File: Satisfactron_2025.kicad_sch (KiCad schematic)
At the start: 147 parts, among them J1 USB-TYPE-C-018, J10 GT-BTP30002-0350B-019B, J11 Conn_01x03, J12 LED strip, J2 GT-BTP30002-0350B-019B, J3 TF_PUSH, J4 GT-BTP30002-0350B-019B, J5 PZ254V-11-04P_C2691448, J6 Conn_01x06, J7 GT-BTP30002-0350B-019B, J8 GT-BTP30002-0350B-019B, J9 GT-BTP30002-0350B-019B, Q1 2N7002, SW1 MSK-22D18G4_051, SW10 SPVN310101, SW11 SPVN310101, SW12 SPVN310101, SW13 SPVN310101, SW14 SPVN310101, SW15 SPVN310101, SW2 TS-1088-AR02016, SW3 SPVN310101, SW4 SPVN310101, SW5 TS-1088-AR02016, SW6 TS-1088-AR02016, SW7 TS-1088-AR02016, SW8 SPVN310101, SW9 SPVN310101, U1 AMS1117-3.3, U10 WS2811C, U11 WS2811C, U12 WS2811C, U13 WS2811C, U14 TSSP77038TT, U2 TPS82130, U3 ESP32-S3-WROOM-1-N16R8, U4 TSSP77038TR, U5 TSSP77038TR, U6 TSSP77038TR, U7 TSSP77038TR, U8 TSSP77038TR, U9 WS2811C

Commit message: Minor corrections
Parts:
- added SW16, SW17, SW18, SW19, SW20: SPVN310101, Switch_KSL:SW-SMD_SPVN310101, symbol Switch_KSL:SPVN310101
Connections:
- no-connect marks 31 -> 51

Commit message: RC last check, silkscreen done
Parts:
- U1: LCSC C7376 -> C6186
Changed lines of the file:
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@@
 			)
 		)
-		(property "LCSC" "C7376"
+		(property "LCSC" "C6186"
 			(at 52.07 161.925 0)
 			(effects

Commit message: Production file (incl. Step)
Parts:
- C18, C19, C20, C21, C24: LCSC (none) -> C14663
- D2: LCSC C2286 -> C2290
- Q1: LCSC (none) -> C8545
- R1, R3: LCSC (none) -> C23186
- R11: LCSC C25804 -> C23162
- R15, R16, R17, R8, R9: LCSC C23182 -> C22808
- R19: LCSC (none) -> C21190
- R21, R22, R26, R32, R33, R34, R35, R36, R37, R38, R39, R40, R41, R42, R5, R6, R7: LCSC C23182 -> C23140
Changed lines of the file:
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@@
 			)
 		)
-		(property "LCSC" "C23182"
+		(property "LCSC" "C22808"
 			(at 288.29 53.34 0)
 			(effects
@@
 			)
 		)
-		(property "LCSC" "C23182"
+		(property "LCSC" "C23140"
 			(at 260.35 58.42 0)
 			(effects
@@
 			)
 		)
-		(property "LCSC" "C23182"
+		(property "LCSC" "C23140"
 			(at 311.15 60.96 0)
 			(effects
@@
 			)
 		)
-		(property "LCSC" "C23182"
+		(property "LCSC" "C23140"
 			(at 360.68 60.96 0)
 			(effects
@@
 			)
 		)
-		(property "LCSC" "C23182"
+		(property "LCSC" "C23140"
 			(at 151.13 58.42 0)
 			(effects
@@
 			)
 		)
-		(property "LCSC" "C23182"
+		(property "LCSC" "C23140"
 			(at 200.66 63.5 0)
 			(effects
@@
 			)
 		)
+		(property "LCSC" "C21190"
+			(at 88.9 255.27 0)
+			(effects
+				(font
+					(size 1.27 1.27)
+				)
+				(hide yes)
+			)
+		)
 		(pin "1"
 		)
@@
 			)
 		)
-		(property "LCSC" "C23182"
+		(property "LCSC" "C22808"
 			(at 233.68 53.34 0)
 			(effects
@@
 			)
 		)
-		(property "LCSC" "C23182"
+		(property "LCSC" "C23140"
 			(at 308.61 63.5 0)
 			(effects
@@
 			)
 		)
-		(property "LCSC" "C23182"
+		(property "LCSC" "C23140"
 			(at 17.78 212.09 0)
 			(effects
@@
 			)
 		)
-		(property "LCSC" "C23182"
+		(property "LCSC" "C23140"
 			(at 205.74 58.42 0)
 			(effects
@@
 			)
 		)
-		(property "LCSC" "C25804"
+		(property "LCSC" "C23162"
 			(at 120.65 195.58 0)
 			(effects
@@
 			)
 		)
+		(property "LCSC" "C14663"
+			(at 295.91 59.6835 0)
+			(effects
+				(font
+					(size 1.27 1.27)
+				)
+				(hide yes)
+			)
+		)
 		(pin "1"
 		)
@@
 			)
 		)
-		(property "LCSC" "C23182"
+		(property "LCSC" "C23140"
 			(at 146.05 63.5 0)
 			(effects
@@
 			)
 		)
+		(property "LCSC" "C8545"
+			(at 141.732 193.548 0)
+			(effects
+				(font
+					(size 1.27 1.27)
+				)
+				(hide yes)
+			)
+		)
 		(pin "3"
 		)
@@
 			)
 		)
-		(property "LCSC" "C23182"
+		(property "LCSC" "C23140"
 			(at 203.2 60.96 0)
 			(effects
@@
 			)
 		)
-		(property "LCSC" "C23182"
+		(property "LCSC" "C22808"
 			(at 391.16 53.34 0)
 			(effects
@@
 			)
 		)
-		(property "LCSC" "C23182"
+		(property "LCSC" "C23140"
 			(at 257.81 60.96 0)
 			(effects
@@
 			)
 		)
+		(property "LCSC" "C14663"
+			(at 349.25 59.6835 0)
+			(effects
+				(font
+					(size 1.27 1.27)
+				)
+				(hide yes)
+			)
+		)
 		(pin "1"
 		)
@@
 			)
 		)
+		(property "LCSC" "C14663"
+			(at 186.69 54.6035 0)
+			(effects
+				(font
+					(size 1.27 1.27)
+				)
+				(hide yes)
+			)
+		)
 		(pin "1"
 		)
@@
 			)
 		)
-		(property "LCSC" "C23182"
+		(property "LCSC" "C22808"
 			(at 179.07 49.53 0)
 			(effects
@@
 			)
 		)
-		(property "LCSC" "C23182"
+		(property "LCSC" "C23140"
 			(at 148.59 60.96 0)
 			(effects
@@
 			)
 		)
-		(property "LCSC" "C23182"
+		(property "LCSC" "C23140"
 			(at 363.22 58.42 0)
 			(effects
@@
 			)
 		)
+		(property "LCSC" "C14663"
+			(at 241.3 59.6835 0)
+			(effects
+				(font
+					(size 1.27 1.27)
+				)
+				(hide yes)
+			)
+		)
 		(pin "1"
 		)
@@
 			)
 		)
-		(property "LCSC" ""
+		(property "LCSC" "C23186"
 			(at 20.32 138.43 0)
 			(effects
@@
 			)
 		)
-		(property "LCSC" "C2286"
+		(property "LCSC" "C2290"
 			(at 76.2 210.82 0)
 			(effects
@@
 			)
 		)
+		(property "LCSC" "C14663"
+			(at 398.78 59.6835 0)
+			(effects
+				(font
+					(size 1.27 1.27)
+				)
+				(hide yes)
+			)
+		)
 		(pin "1"
 		)
@@
 			)
 		)
-		(property "LCSC" "C23182"
+		(property "LCSC" "C23140"
 			(at 392.43 73.66 0)
 			(effects
@@
 			)
 		)
-		(property "LCSC" "C23182"
+		(property "LCSC" "C23140"
 			(at 313.69 58.42 0)
 			(effects
@@
 			)
 		)
-		(property "LCSC" "C23182"
+		(property "LCSC" "C22808"
 			(at 341.63 53.34 0)
 			(effects
@@
 			)
 		)
-		(property "LCSC" "C23182"
+		(property "LCSC" "C23140"
 			(at 358.14 63.5 0)
 			(effects
@@
 			)
 		)
-		(property "LCSC" "C23182"
+		(property "LCSC" "C23140"
 			(at 255.27 63.5 0)
 			(effects
@@
 			)
 		)
-		(property "LCSC" ""
+		(property "LCSC" "C23186"
 			(at 67.31 138.43 0)
 			(effects

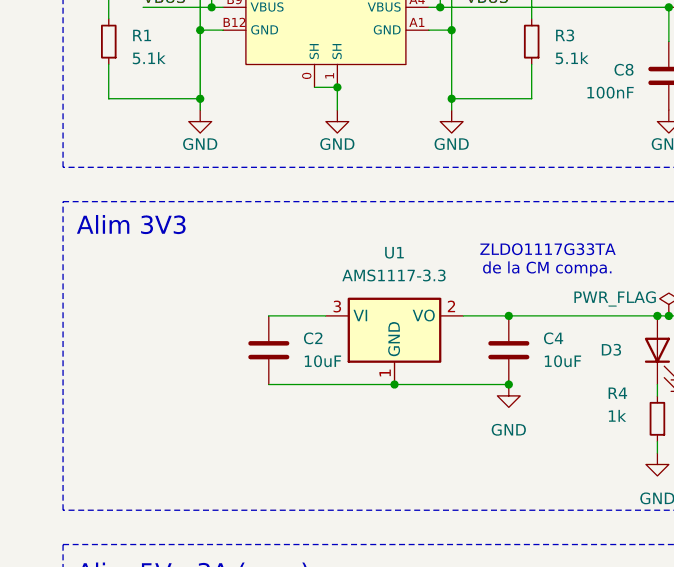
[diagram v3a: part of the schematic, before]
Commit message: Correct major issue on schematics, 5V in missing on 3V3 reg TODO PCB
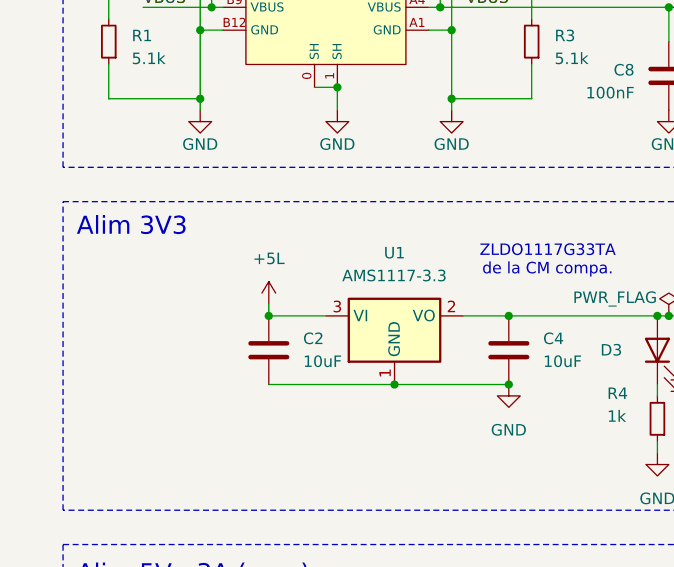
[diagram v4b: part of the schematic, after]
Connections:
- net +5L: now also C2.1, U1.3 (VI)
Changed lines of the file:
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@@
 	)
 	(junction
+		(at 38.1 168.91)
+		(diameter 0)
+		(color 0 0 0 0)
+	)
+	(junction
 		(at 292.1 228.6)
 		(diameter 0)
@@
 	(wire
 		(pts
+			(xy 38.1 167.64) (xy 38.1 168.91)
+		)
+		(stroke
+			(width 0)
+			(type default)
+		)
+	)
+	(wire
+		(pts
 			(xy 146.05 66.04) (xy 152.4 66.04)
 		)
@@
 					(unit 1)
 				)
+			)
+		)
+	)
+	(symbol
+		(lib_id "power:+5VP")
+		(at 38.1 167.64 0)
+		(unit 1)
+		(exclude_from_sim no)
+		(in_bom yes)
+		(on_board yes)
+		(dnp no)
+		(fields_autoplaced yes)
+		(property "Reference" "#PWR084"
+			(at 38.1 171.45 0)
+			(effects
+				(font
+					(size 1.27 1.27)
+				)
+				(hide yes)
+			)
+		)
+		(property "Value" "+5L"
+			(at 38.1 162.56 0)
+			(effects
+				(font
+					(size 1.27 1.27)
+				)
+			)
+		)
+		(property "Footprint" ""
+			(at 38.1 167.64 0)
+			(effects
+				(font
+					(size 1.27 1.27)
+				)
+				(hide yes)
+			)
+		)
+		(property "Datasheet" ""
+			(at 38.1 167.64 0)
+			(effects
+				(font
+					(size 1.27 1.27)
+				)
+				(hide yes)
+			)
+		)
+		(property "Description" ""
+			(at 38.1 167.64 0)
+			(effects
+				(font
+					(size 1.27 1.27)
+				)
+				(hide yes)
+			)
+		)
+		(pin "1"
+		)
+		(instances
+			(project "Satisfactron_2025"
+				(path "/d0b6cc72-ff07-4f5e-a148-04b65c86a715"
+					(reference "#PWR084")
+					(unit 1)
+				)
